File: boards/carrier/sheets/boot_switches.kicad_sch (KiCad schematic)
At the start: 8 parts

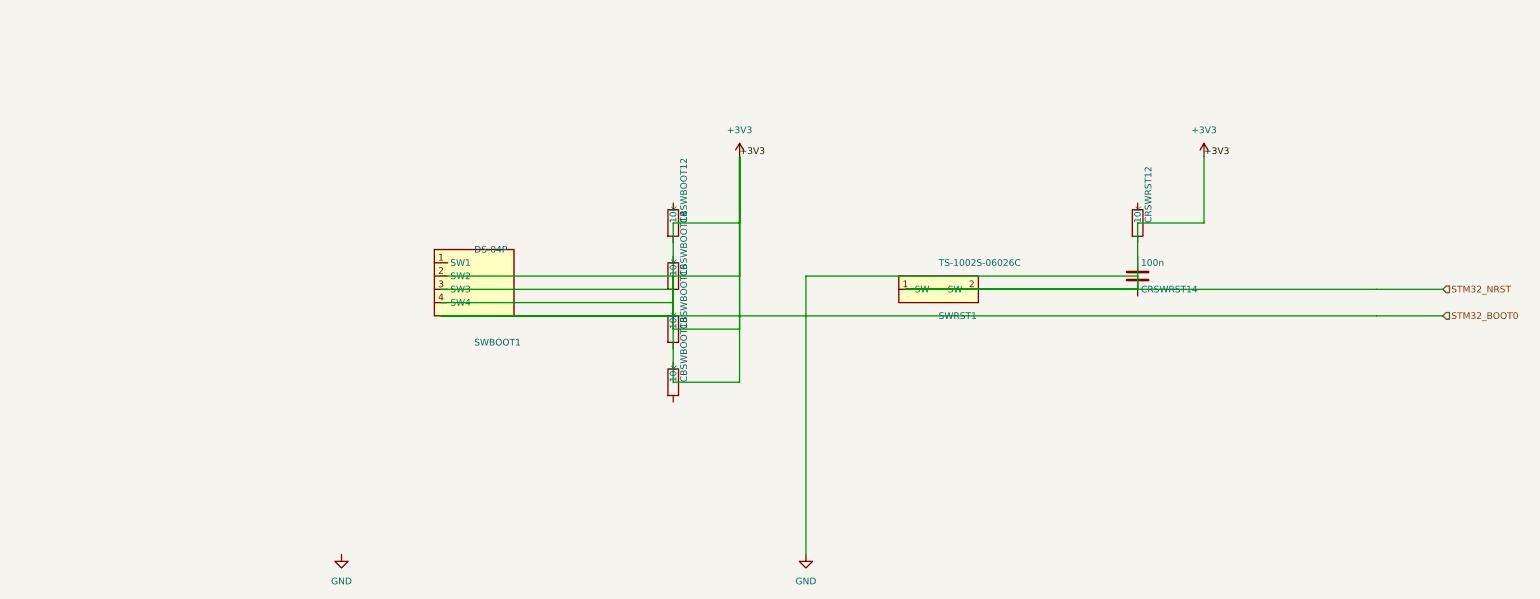
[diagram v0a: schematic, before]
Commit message: Stage 6 (2/4): add microsd, boot_switches, jtag_swd blocks (skip aux_io, xadc_clk)
  * microsd: Hirose DM3AT-SF-PEJM5 push-push socket on Zynq PS SD1 (4-bit
    SDIO + dedicated card-detect via DET_A/DET_B). Uses KiCad built-in
    Connector:Micro_SD_Card_Det_Hirose_DM3AT symbol; VDD decoupling and
    DAT[0..3]/CMD pull-ups come from MICROSD_DM3AT_REFCIRCUIT.

  * boot_switches: SW1 4-pos DIP (ZYNQ_BOOT_MODE[3:0] straps with 10k
    pull-ups from DIP_SWITCH_REFCIRCUIT) + SW2 tactile (ZYNQ_PS_SRST_N
    with pull-up + debounce from TACTILE_SWITCH_REFCIRCUIT).

  * jtag_swd: J1 Zynq PS JTAG 2x7 (UG470 Xilinx 6-wire pinout, no TRST
    pin in the JTAG_2x7 symbol) + J2 STM32 SWD 2x5 (ARM Cortex 10-pin
    with SWDIO/nRESET pull-ups from SWD_HEADER_REFCIRCUIT).

  * aux_io and xadc_clk skipped: no refcircuit exists for AUX_GPIO_IO
    or XADC_MRCC_IO connectors, and authoring new refcircuits is
    out of scope per task instructions.

$ python -m zynq_eda --board carrier
built 5 block(s): power, usb_pd, microsd, boot_switches, jtag_swd

Co-Authored-By: Claude Opus 4.7 <noreply@anthropic.com>
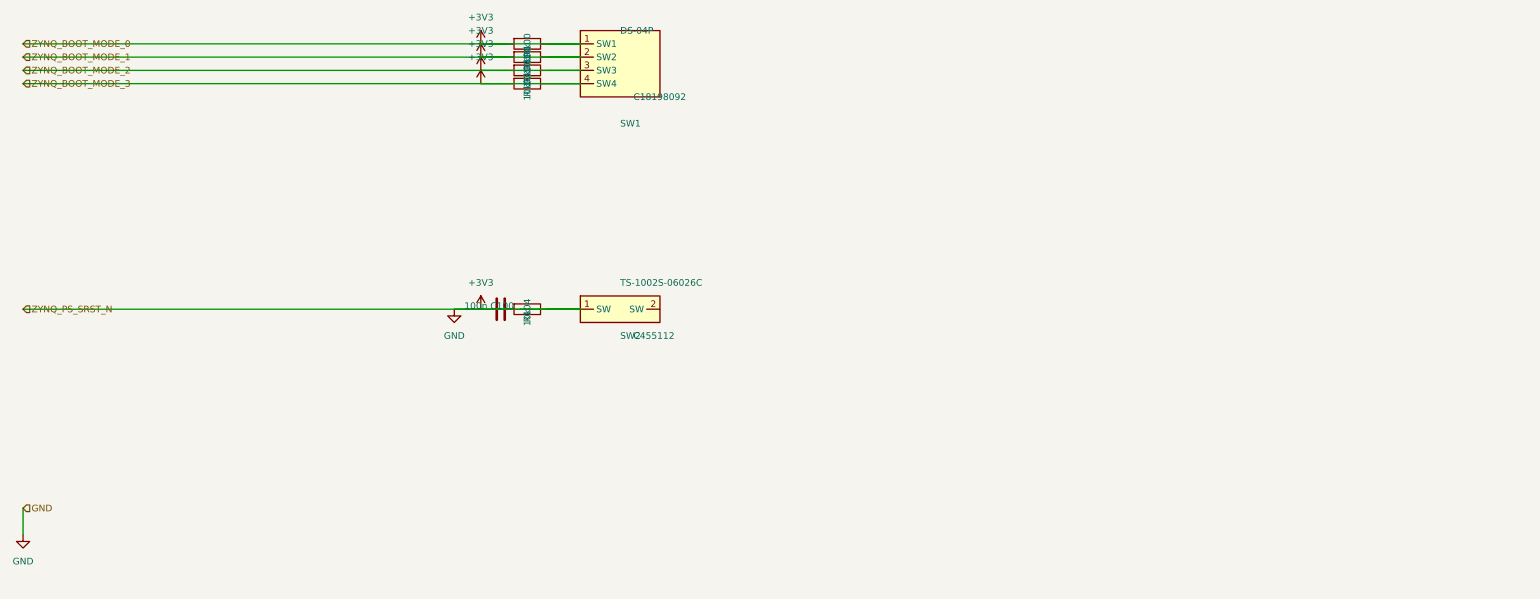
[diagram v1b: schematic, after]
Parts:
- removed CBSWBOOT12, CBSWBOOT14, CBSWBOOT16, CBSWBOOT18, CRSWRST12: 10k, Resistor_SMD:R_0402_1005Metric, symbol Device:R
- removed CRSWRST14: 100n, Capacitor_SMD:C_0402_1005Metric, symbol Device:C
- removed SWBOOT1: DS-04P, Switch_SMD:DIP_Switch_x4, symbol carrier:SW_DIP_4
- removed SWRST1: TS-1002S-06026C, Button_Switch_SMD:SW_SPST_Tactile_6x6mm, symbol carrier:SW_TACT
- added C100: 100n, Capacitor_SMD:C_0402_1005Metric, symbol Device:C
- added R100, R101, R102, R103, R104: 10k, Resistor_SMD:R_0402_1005Metric, symbol Device:R
- added SW1: DS-04P, Switch_SMD:DIP_Switch_x4, symbol zynq_eda:SW_DIP_4
- added SW2: TS-1002S-06026C, Button_Switch_SMD:SW_SPST_Tactile_6x6mm, symbol zynq_eda:SW_TACT
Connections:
- net +3V3: now also C100.1, C100.2, R100.1, R100.2, R101.1, R101.2, R102.1, R102.2, R103.1, R103.2, R104.1, R104.2, SW1.1 (SW1), SW1.2 (SW2), SW1.3 (SW3), SW1.4 (SW4), SW2.1 (SW)
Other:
- title: Boot Mode + Reset Switches -> Boot Mode Straps + PS Reset (DIP-4 + Tactile)
